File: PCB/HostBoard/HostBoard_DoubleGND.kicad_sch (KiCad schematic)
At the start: 23 parts, among them J1 Conn_01x06, J10 Conn_01x05, J11 Screw_Terminal_01x02, J12 Conn_02x07_Odd_Even, J2 Conn_01x03, J3 Conn_01x06, J4 Conn_01x03, J5 Conn_01x06, J6 Conn_01x04, J7 Conn_01x04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

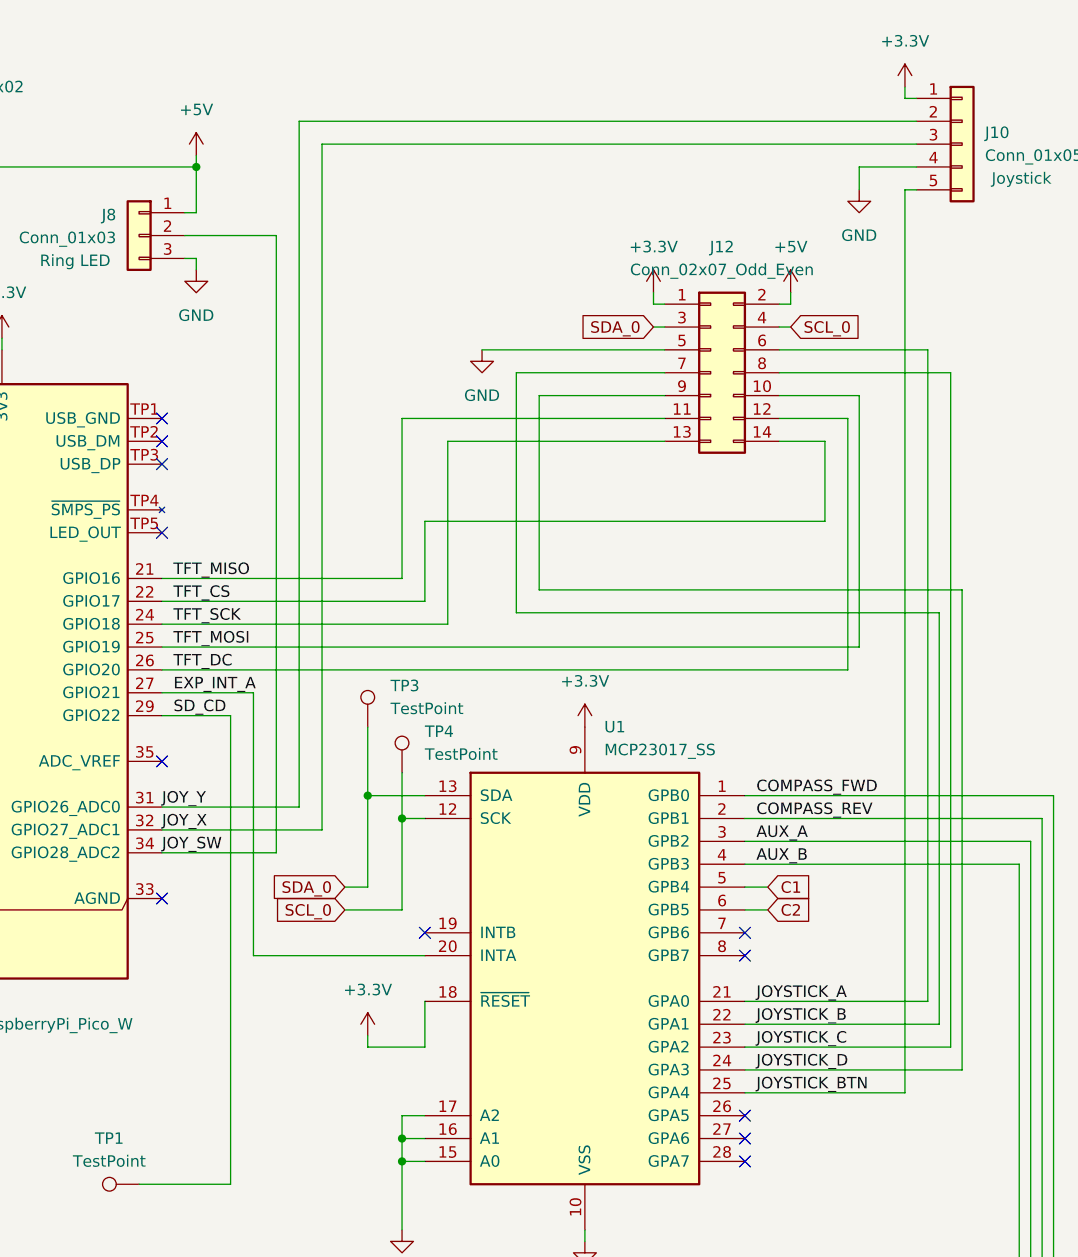
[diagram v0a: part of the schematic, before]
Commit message: Add new PCB layout with two ground planes, no power planes, routing in N-S and E-W on top and bottom
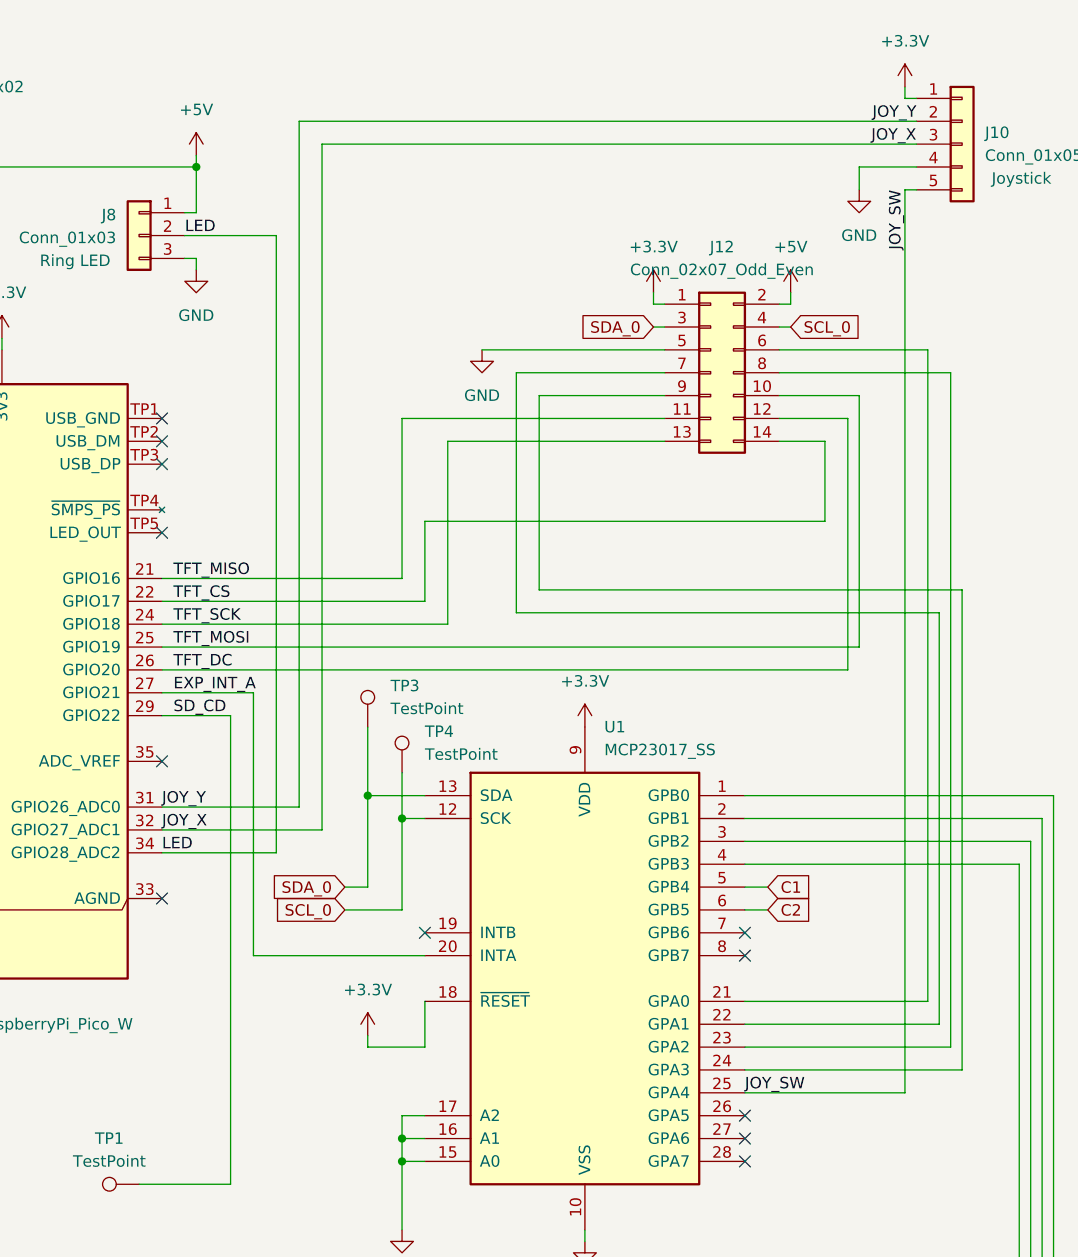
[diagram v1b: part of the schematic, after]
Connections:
- net JOYSTICK_BTN is gone; now on net JOY_SW: J10.5 (Pin_5), U1.25 (GPA4)
- net JOY_SW: no longer A1.34 (GPIO28_ADC2), J8.2 (Pin_2)
- net AUX_A: no longer names the net of U1.3 (GPB2), U3.22 (AIN2)
- net AUX_B: no longer names the net of U1.4 (GPB3), U3.21 (AIN1)
- net COMPASS_FWD: no longer names the net of U1.1 (GPB0), U3.16 (BIN2)
- net COMPASS_REV: no longer names the net of U1.2 (GPB1), U3.17 (BIN1)
- net JOYSTICK_A: no longer names the net of J12.6 (Pin_6), U1.21 (GPA0)
- net JOYSTICK_B: no longer names the net of J12.7 (Pin_7), U1.22 (GPA1)
- net JOYSTICK_C: no longer names the net of J12.8 (Pin_8), U1.23 (GPA2)
- net JOYSTICK_D: no longer names the net of J12.9 (Pin_9), U1.24 (GPA3)
- new net LED: A1.34 (GPIO28_ADC2), J8.2 (Pin_2)
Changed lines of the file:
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@@
-	(wire
-		(pts
-			(xy 264.16 33.02) (xy 262.89 33.02)
-		)
-		(stroke
-			(width 0)
-			(type default)
-		)
-	)
 	(wire
 		(pts
@@
 	(wire
 		(pts
+			(xy 262.89 133.35) (xy 245.11 133.35)
+		)
+		(stroke
+			(width 0)
+			(type default)
+		)
+	)
+	(wire
+		(pts
 			(xy 36.83 156.21) (xy 45.72 156.21)
 		)
@@
 	(wire
 		(pts
-			(xy 245.11 133.35) (xy 262.89 133.35)
-		)
-		(stroke
-			(width 0)
-			(type default)
-		)
-	)
-	(wire
-		(pts
 			(xy 157.48 30.48) (xy 184.15 30.48)
 		)
@@
 	(wire
 		(pts
+			(xy 262.89 33.02) (xy 264.16 33.02)
+		)
+		(stroke
+			(width 0)
+			(type default)
+		)
+	)
+	(wire
+		(pts
 			(xy 116.84 128.27) (xy 116.84 129.54)
 		)
@@
 			(width 0)
 			(type default)
-		)
-	)
-	(label "COMPASS_FWD"
-		(at 246.38 100.33 0)
-		(effects
-			(font
-				(size 1.27 1.27)
-			)
-			(justify left bottom)
 		)
 	)
@@
 		)
 	)
+	(label "LED"
+		(at 180.34 106.68 0)
+		(effects
+			(font
+				(size 1.27 1.27)
+			)
+			(justify left bottom)
+		)
+	)
+	(label "JOY_SW"
+		(at 245.11 133.35 0)
+		(effects
+			(font
+				(size 1.27 1.27)
+			)
+			(justify left bottom)
+		)
+	)
 	(label "EXP_INT_A"
 		(at 181.61 88.9 0)
@@
 		)
 	)
+	(label "LED"
+		(at 182.88 38.1 0)
+		(effects
+			(font
+				(size 1.27 1.27)
+			)
+			(justify left bottom)
+		)
+	)
+	(label "JOY_Y"
+		(at 264.16 25.4 180)
+		(effects
+			(font
+				(size 1.27 1.27)
+			)
+			(justify right bottom)
+		)
+	)
 	(label "JOY_X"
 		(at 180.34 104.14 0)
@@
 	)
 	(label "JOY_SW"
-		(at 180.34 106.68 0)
-		(effects
-			(font
-				(size 1.27 1.27)
-			)
-			(justify left bottom)
+		(at 262.89 33.02 270)
+		(effects
+			(font
+				(size 1.27 1.27)
+			)
+			(justify right bottom)
 		)
 	)
@@
 		)
 	)
-	(label "JOYSTICK_A"
-		(at 246.38 123.19 0)
-		(effects
-			(font
-				(size 1.27 1.27)
-			)
-			(justify left bottom)
-		)
-	)
 	(label "TFT_MISO"
 		(at 181.61 76.2 0)
@@
 		)
 	)
-	(label "AUX_B"
-		(at 246.38 107.95 0)
-		(effects
-			(font
-				(size 1.27 1.27)
-			)
-			(justify left bottom)
-		)
-	)
 	(label "AZIMUTH_CHA"
 		(at 133.35 99.06 180)
@@
 		)
 	)
-	(label "JOYSTICK_B"
-		(at 246.38 125.73 0)
-		(effects
-			(font
-				(size 1.27 1.27)
-			)
-			(justify left bottom)
-		)
-	)
 	(label "ELEVATION_IDX"
 		(at 133.35 104.14 180)
@@
 		)
 	)
+	(label "JOY_X"
+		(at 264.16 27.94 180)
+		(effects
+			(font
+				(size 1.27 1.27)
+			)
+			(justify right bottom)
+		)
+	)
 	(label "AZIMUTH_FWD"
 		(at 133.35 93.98 180)
@@
 		)
 	)
-	(label "AUX_A"
-		(at 246.38 105.41 0)
-		(effects
-			(font
-				(size 1.27 1.27)
-			)
-			(justify left bottom)
-		)
-	)
 	(label "ELEVATION_CHA"
 		(at 133.35 78.74 180)
@@
 		)
 	)
-	(label "JOYSTICK_C"
-		(at 246.38 128.27 0)
-		(effects
-			(font
-				(size 1.27 1.27)
-			)
-			(justify left bottom)
-		)
-	)
 	(label "TFT_SCK"
 		(at 181.61 81.28 0)
-		(effects
-			(font
-				(size 1.27 1.27)
-			)
-			(justify left bottom)
-		)
-	)
-	(label "JOYSTICK_BTN"
-		(at 246.38 133.35 0)
-		(effects
-			(font
-				(size 1.27 1.27)
-			)
-			(justify left bottom)
-		)
-	)
-	(label "JOYSTICK_D"
-		(at 246.38 130.81 0)
-		(effects
-			(font
-				(size 1.27 1.27)
-			)
-			(justify left bottom)
-		)
-	)
-	(label "COMPASS_REV"
-		(at 246.38 102.87 0)
 		(effects
 			(font
@@
 	)
 	(symbol
-		(lib_name "TB6612FNG_1")
 		(lib_id "Driver_Motor:TB6612FNG")
 		(at 93.98 156.21 0)

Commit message: As sent to JLBPCB. $66.
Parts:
- added J13: Conn_01x02, Connector_PinHeader_2.54mm:PinHeader_1x02_P2.54mm_Vertical, symbol Connector_Generic:Conn_01x02
- added TP2: 5V, Connector_PinHeader_2.54mm:PinHeader_1x01_P2.54mm_Vertical, symbol Connector:TestPoint
- added TP5: 3V3, Connector_PinHeader_2.54mm:PinHeader_1x01_P2.54mm_Vertical, symbol Connector:TestPoint
- added TP6: CL_A, TestPoint:TestPoint_Pad_1.0x1.0mm, symbol Connector:TestPoint
- added TP7: CL_B, TestPoint:TestPoint_Pad_1.0x1.0mm, symbol Connector:TestPoint
- TP1: value TestPoint -> SD_DC
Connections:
- net +3.3V: now also TP5.1
- net +5V: now also TP2.1
- net GND: now also A1.33 (AGND)
- net at U2.11 (BO1), U2.12 (BO1): now also J3.6 (Pin_6); no longer J3.1 (Pin_1)
- net at U2.7 (BO2), U2.8 (BO2): now also J3.1 (Pin_1); no longer J3.6 (Pin_6)
- net GP14: now reaches A1.19 (GPIO14)
- net GP14: now also J13.1 (Pin_1)
- net GP15: now reaches A1.20 (GPIO15)
- net GP15: now also J13.2 (Pin_2)
- net COMPASS_LIMIT_A: now reaches U1.7 (GPB6)
- net COMPASS_LIMIT_A: now also TP6.1
- net COMPASS_LIMIT_B: now reaches U1.8 (GPB7)
- net COMPASS_LIMIT_B: now also TP7.1
- net SD_CD renamed SD_DC
- no-connect marks 19 -> 16
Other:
- moved on the sheet: C1, C2
